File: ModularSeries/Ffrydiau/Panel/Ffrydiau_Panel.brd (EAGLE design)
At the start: 50.5 x 128.5 mm, 15 parts

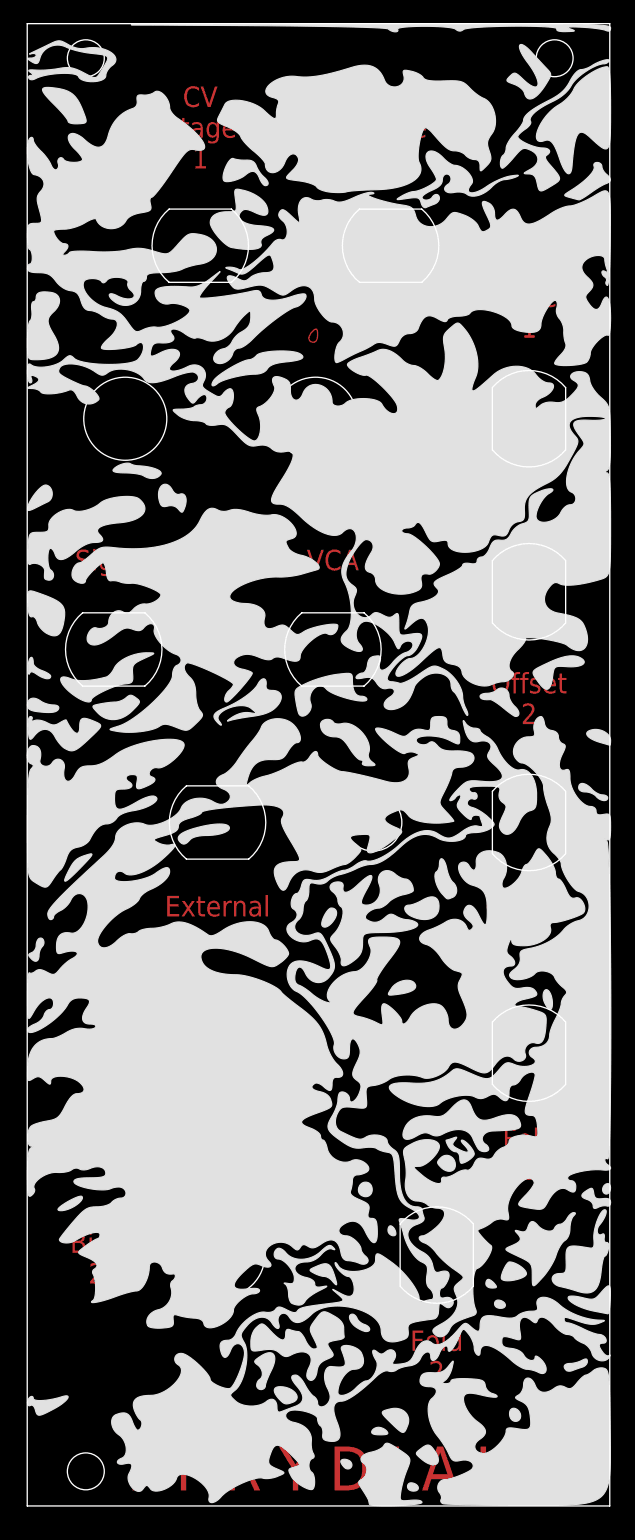
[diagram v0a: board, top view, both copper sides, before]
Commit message: Layout and schematic renders for LHP added
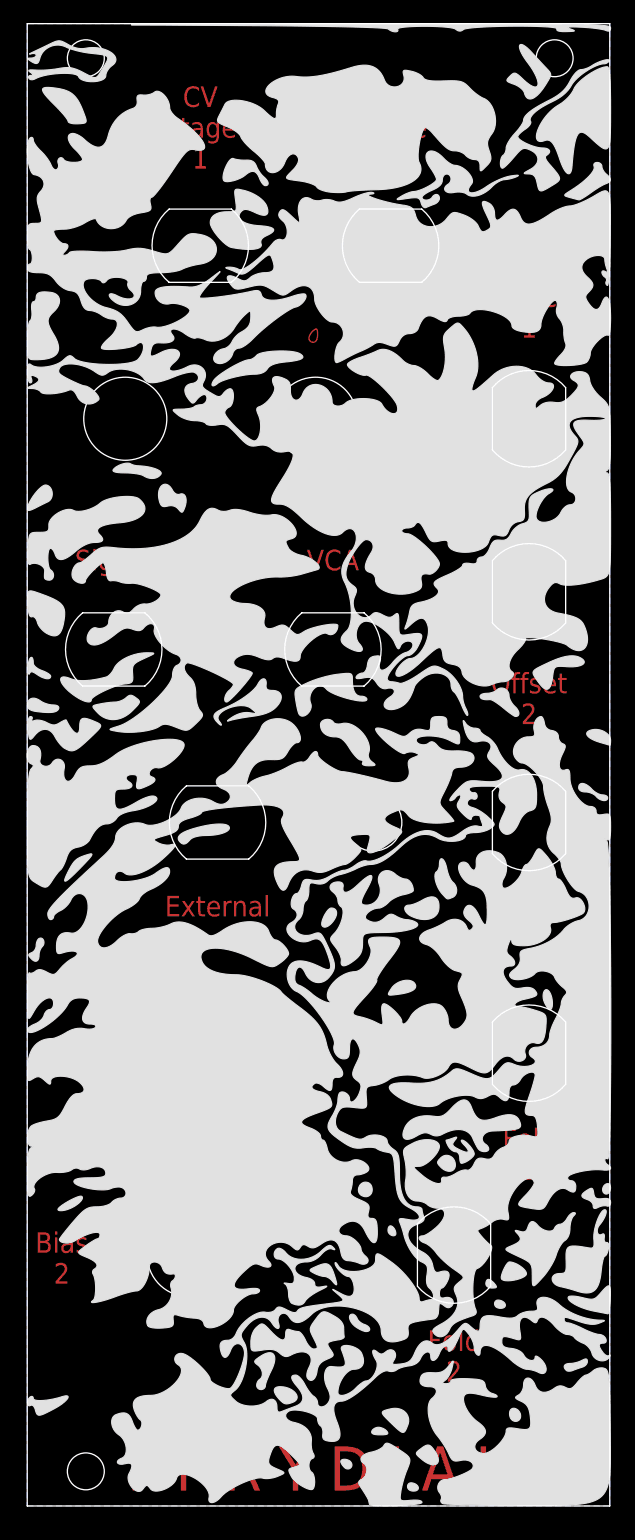
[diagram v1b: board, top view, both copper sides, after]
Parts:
- moved E$14 3.00 mm to (14.0, 21.8)
- moved E$10 1.50 mm to (37.0, 21.8)
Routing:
- added copper zone on layer 16, net GND
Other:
- board text added: "LAYERS"
- board text added: "PLEATS"
- board text added: "WRINKLES"
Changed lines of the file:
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@@
 <layer number="21" name="tPlace" color="7" fill="1" visible="yes" active="yes"/>
 <layer number="22" name="bPlace" color="7" fill="1" visible="no" active="yes"/>
-<layer number="23" name="tOrigins" color="15" fill="1" visible="no" active="yes"/>
+<layer number="23" name="tOrigins" color="15" fill="1" visible="yes" active="yes"/>
 <layer number="24" name="bOrigins" color="15" fill="1" visible="no" active="yes"/>
 <layer number="25" name="tNames" color="7" fill="1" visible="no" active="yes"/>
@@
 </layers>
 <board>
+<fusionsync huburn="a.cGVyc29uYWw6dWUyYjdlNGE0" projecturn="a.cGVyc29uYWw6dWUyYjdlNGE0IzIwMjAwNDA1MjgzMzA0MTgx" f3durn="urn:adsk.wipprod:dm.lineage:Q-XySQOaRu-O10WKwIGk7A" pcbguid="" lastpulledtime="" lastsyncedchangeguid="" latestrevisionid="43511777-5243-46b8-b356-505c998e44e2" lastsyncedrevisionid="43511777-5243-46b8-b356-505c998e44e2" lastboardhashguid="3060c261-bfa2-1153-4ef1-e553b7d6a96d" lastpushedtime="2020-07-16T15:10:59Z" linktopcb3d="true"/>
 <plain>
 <wire x1="0" y1="0" x2="50.5" y2="0" width="0" layer="20"/>
@@
 <text x="16.5" y="52" size="1.778" layer="29" font="vector" ratio="12" align="center">External</text>
 <text x="43.5" y="52" size="1.778" layer="29" font="vector" ratio="12" align="center">Output</text>
-<text x="35.5" y="13" size="1.778" layer="29" font="vector" ratio="12" align="center">Fold
+<text x="37" y="13" size="1.778" layer="29" font="vector" ratio="12" align="center">Fold
 2</text>
 <text x="43.5" y="30.5" size="1.778" layer="29" font="vector" ratio="12" align="center">Fold
@@
 <text x="9.5" y="39" size="1.778" layer="29" font="vector" ratio="12" align="center">Bias
 1</text>
-<text x="6" y="21.5" size="1.778" layer="29" font="vector" ratio="12" align="center">Bias
+<text x="3" y="21.5" size="1.778" layer="29" font="vector" ratio="12" align="center">Bias
 2</text>
 <polygon width="0.1" layer="21">
@@
 <text x="16.5" y="52" size="1.778" layer="1" font="vector" ratio="12" align="center">External</text>
 <text x="43.5" y="52" size="1.778" layer="1" font="vector" ratio="12" align="center">Output</text>
-<text x="35.5" y="13" size="1.778" layer="1" font="vector" ratio="12" align="center">Fold
+<text x="37" y="13" size="1.778" layer="1" font="vector" ratio="12" align="center">Fold
 2</text>
 <text x="43.5" y="30.5" size="1.778" layer="1" font="vector" ratio="12" align="center">Fold
@@
 <text x="9.5" y="39" size="1.778" layer="1" font="vector" ratio="12" align="center">Bias
 1</text>
-<text x="6" y="21.5" size="1.778" layer="1" font="vector" ratio="12" align="center">Bias
+<text x="3" y="21.5" size="1.778" layer="1" font="vector" ratio="12" align="center">Bias
 2</text>
+<text x="49" y="17.5" size="1.778" layer="29" font="vector" ratio="12" rot="R90" align="center">WRINKLES</text>
+<text x="1.5" y="59.5" size="1.778" layer="29" font="vector" ratio="12" rot="SR270" align="center">PLEATS</text>
+<text x="49" y="114.5" size="1.778" layer="29" font="vector" ratio="12" rot="R90" align="center">LAYERS</text>
 </plain>
 <attributes>
@@
 <element name="E$8" library="ElectricNoodleBox" package="CINCH_BANANA_CUTOUT" value="" x="43.5" y="59.25" smashed="yes"/>
 <element name="E$9" library="ElectricNoodleBox" package="CINCH_BANANA_CUTOUT" value="" x="43.5" y="39.25" smashed="yes"/>
-<element name="E$10" library="ElectricNoodleBox" package="CINCH_BANANA_CUTOUT" value="" x="35.5" y="21.75" smashed="yes"/>
+<element name="E$10" library="ElectricNoodleBox" package="CINCH_BANANA_CUTOUT" value="" x="37" y="21.75" smashed="yes"/>
 <element name="E$11" library="ElectricNoodleBox" package="ALPHA9MM_POT_CUTOUT" value="" x="25" y="94.25" smashed="yes"/>
 <element name="E$12" library="ElectricNoodleBox" package="ALPHA9MM_POT_CUTOUT" value="" x="8.5" y="94.25" smashed="yes"/>
 <element name="E$13" library="ElectricNoodleBox" package="ALPHA9MM_POT_CUTOUT" value="" x="20.5" y="39.25" smashed="yes"/>
-<element name="E$14" library="ElectricNoodleBox" package="ALPHA9MM_POT_CUTOUT" value="" x="17" y="21.75" smashed="yes"/>
+<element name="E$14" library="ElectricNoodleBox" package="ALPHA9MM_POT_CUTOUT" value="" x="14" y="21.75" smashed="yes"/>
 <element name="E$15" library="ElectricNoodleBox" package="DW1_SWITCH_CUTOUT" value="" x="30" y="59.25" smashed="yes"/>
 </elements>
@@
 </polygon>
 </signal>
+<signal name="GND">
+<polygon width="0.1524" layer="16">
+<vertex x="0" y="0"/>
+<vertex x="50.5" y="0"/>
+<vertex x="50.5" y="128.5"/>
+<vertex x="0" y="128.5"/>
+</polygon>
+</signal>
 </signals>
 <mfgpreviewcolors>
@@
 which will not be processed correctly with this version.
 </note>
+<note version="8.3" severity="warning">
+Since Version 8.3, EAGLE supports Fusion synchronisation.
+This feature will not be available in this version and saving
+the document will break the link to the Fusion PCB feature.
+</note>
 </compatibility>
